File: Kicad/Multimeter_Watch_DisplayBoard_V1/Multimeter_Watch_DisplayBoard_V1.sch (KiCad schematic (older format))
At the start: 14 parts, among them J4 Conn_01x16_Female, J5 Conn_01x16_Female, Q1 A03400A N-MOS

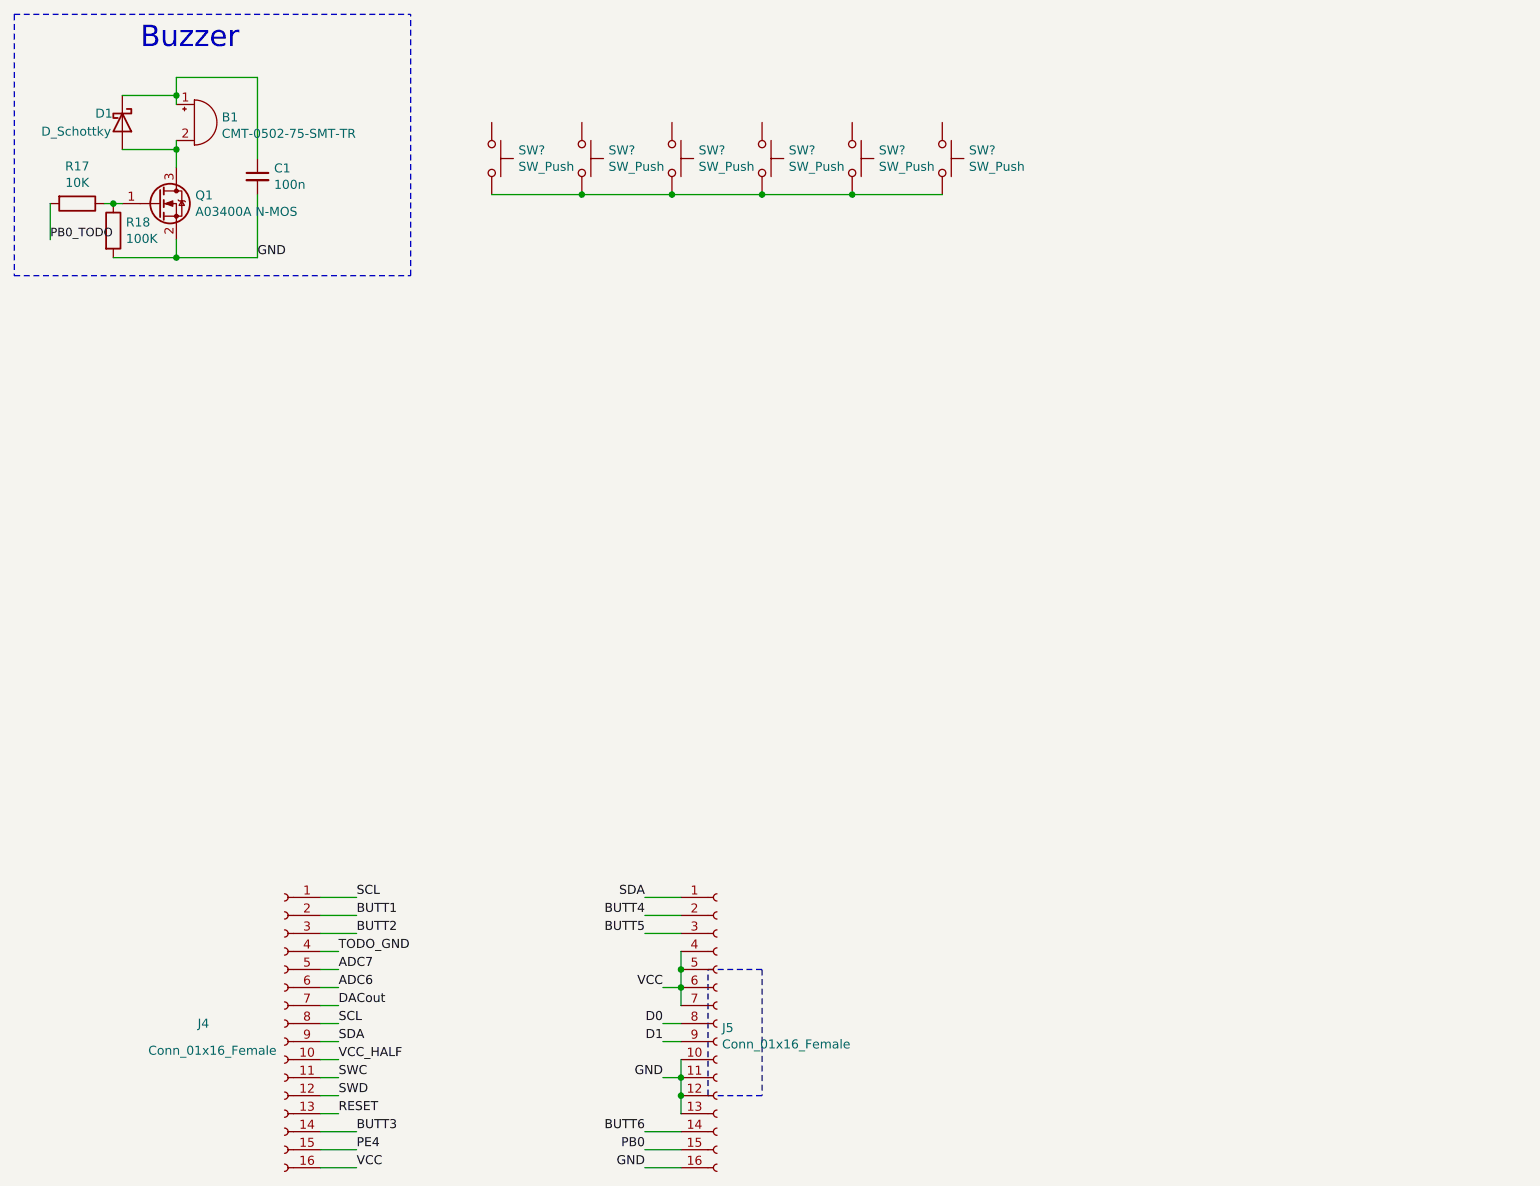
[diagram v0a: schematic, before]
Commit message: measure header distance by center of hole (courtyards are not symmetrical)
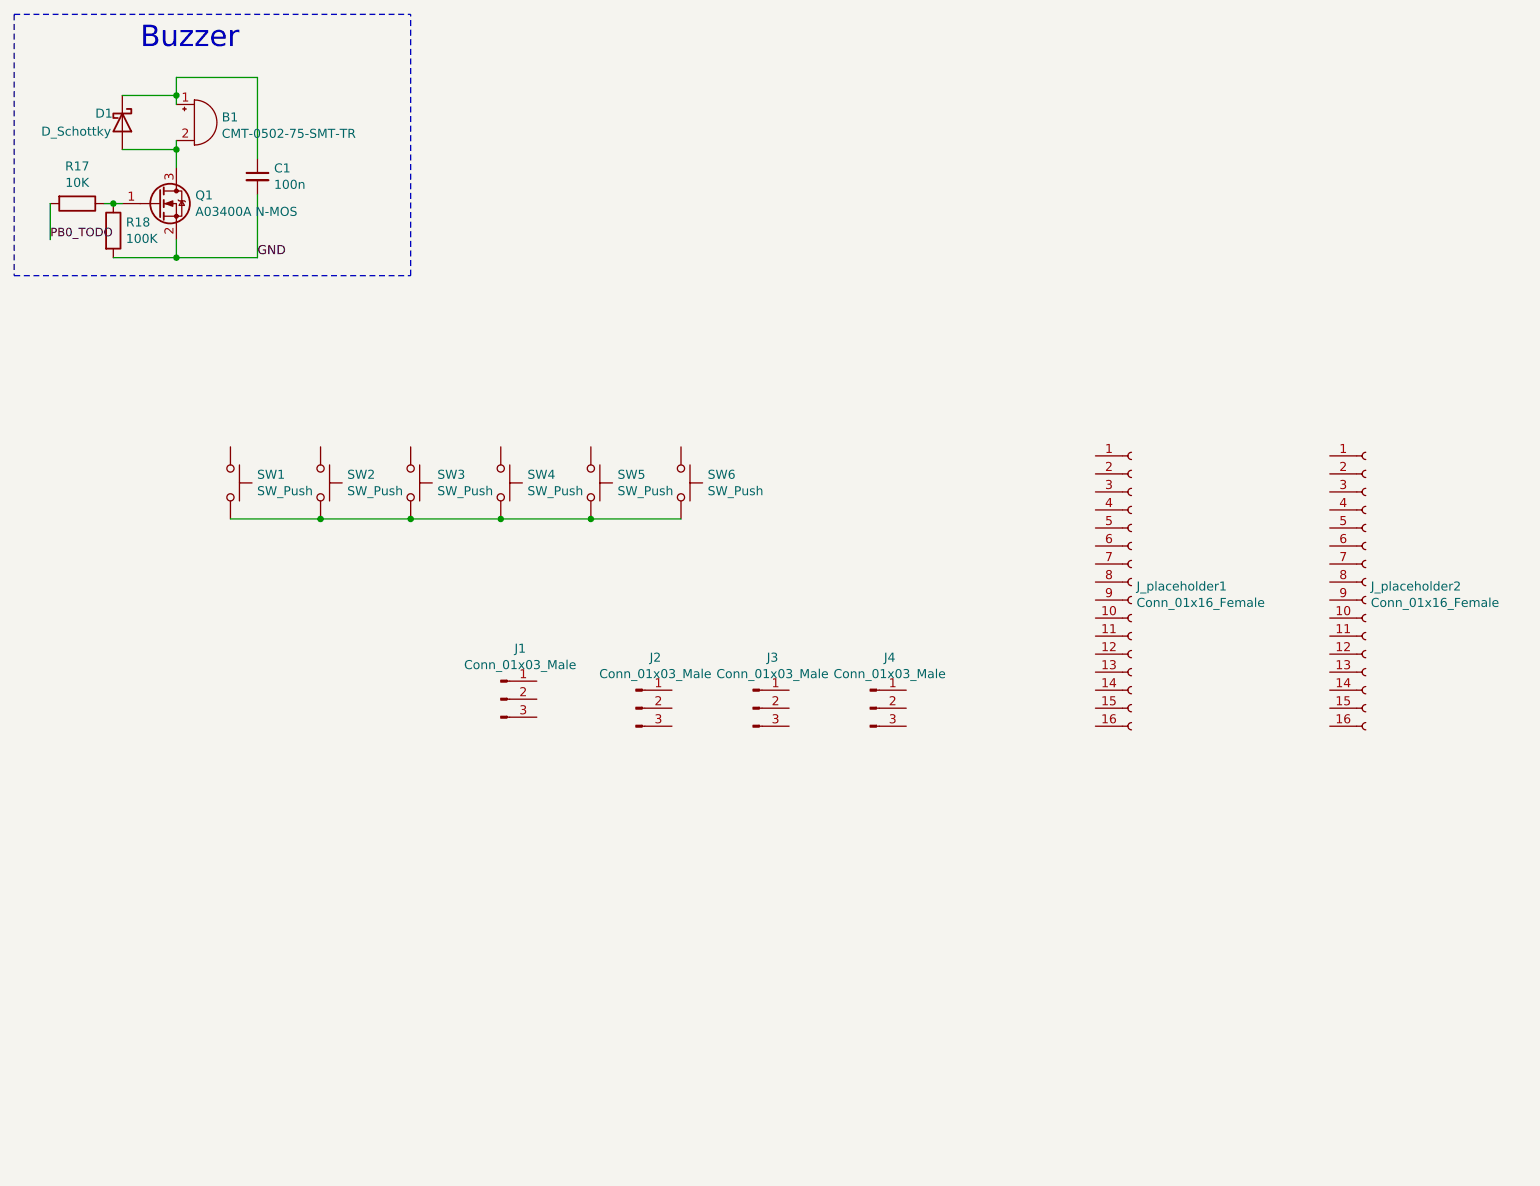
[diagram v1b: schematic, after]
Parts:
- removed J4, J5: Conn_01x16_Female, Connector_PinSocket_2.54mm:PinSocket_1x16_P2.54mm_Vertical, symbol Connector:Conn_01x16_Female
- added J1, J2, J3, J4: Conn_01x03_Male, Connector_PinSocket_2.54mm:PinSocket_1x03_P2.54mm_Vertical, symbol Connector:Conn_01x03_Male
- added J_placeholder1, J_placeholder2: Conn_01x16_Female, Connector_PinSocket_2.54mm:PinSocket_1x16_P2.54mm_Vertical, symbol Connector:Conn_01x16_Female
- gave numbers to parts that had none: 6
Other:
- moved on the sheet: SW1, SW2, SW3, SW4, SW5, SW6

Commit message: display board done, todo: move display down to allow for jack labels
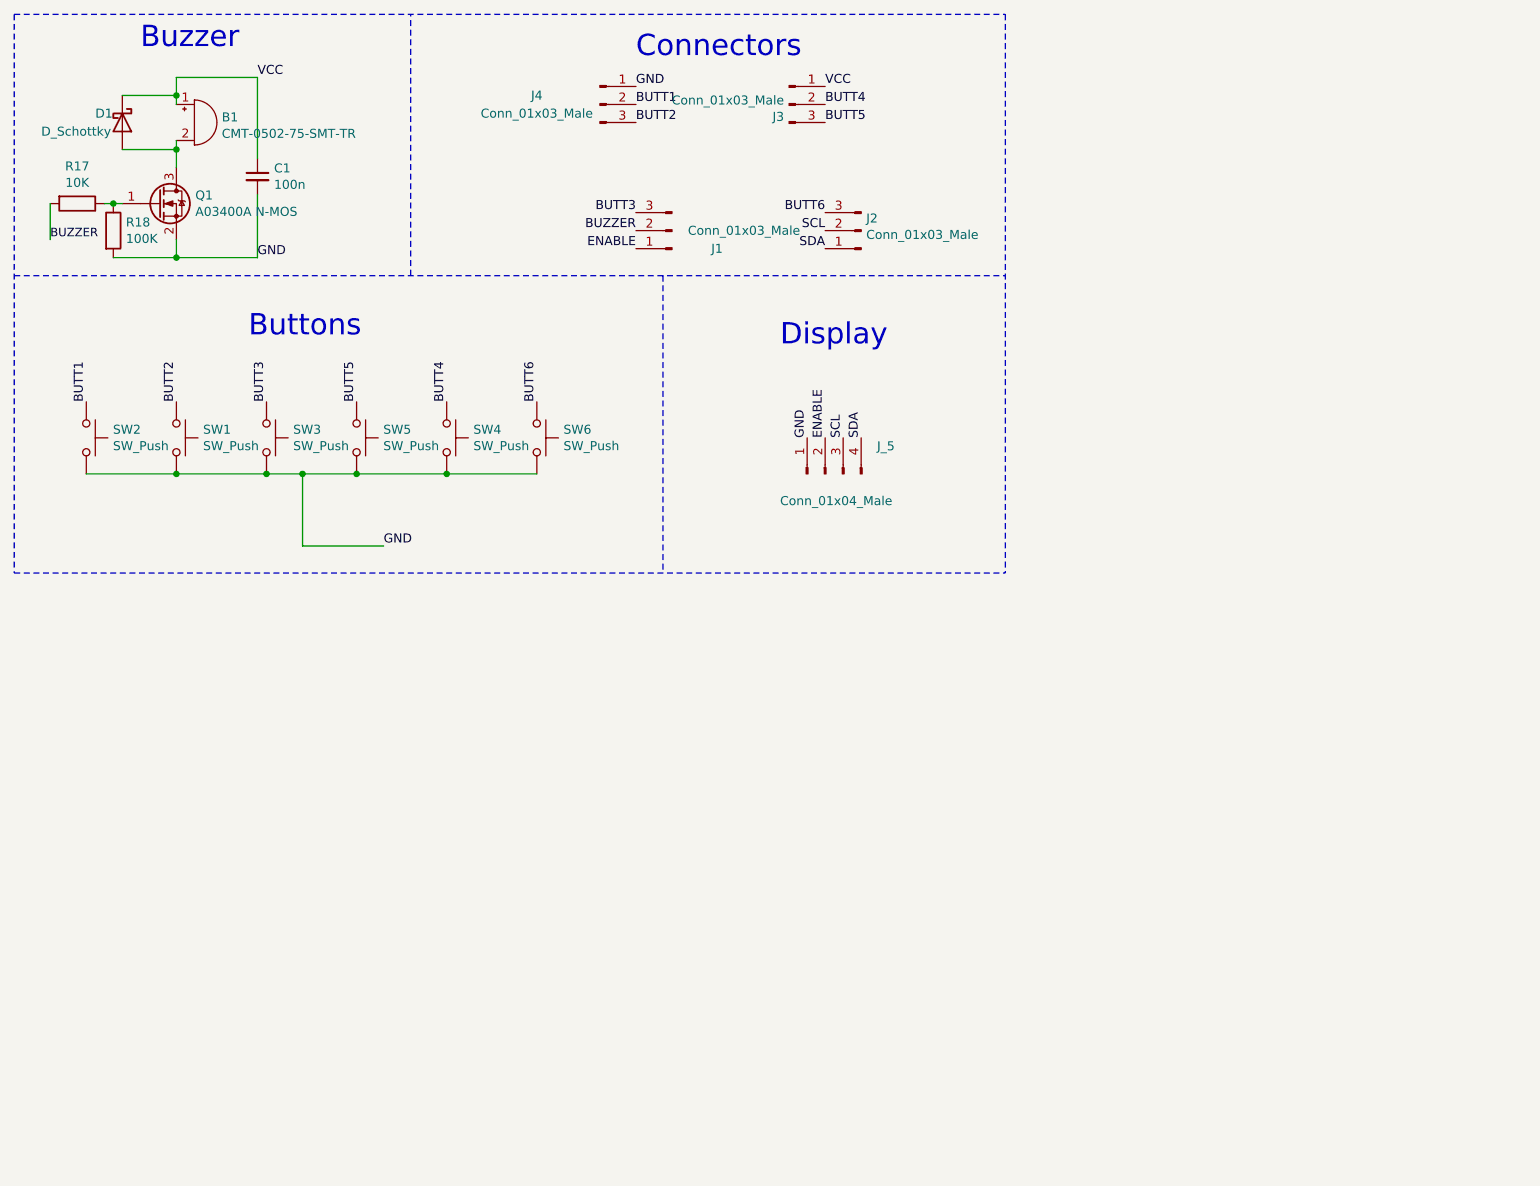
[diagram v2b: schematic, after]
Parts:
- removed J_placeholder1, J_placeholder2: Conn_01x16_Female, Connector_PinSocket_2.54mm:PinSocket_1x16_P2.54mm_Vertical, symbol Connector:Conn_01x16_Female
- added J_5: Conn_01x04_Male, Connector_PinSocket_2.54mm:PinSocket_1x04_P2.54mm_Vertical, symbol Connector:Conn_01x04_Male
- B1: footprint (none) -> Multimeter_Watch_custom_footprints:CMT-0502-75-SMT-TR
- C1: footprint (none) -> Capacitor_SMD:C_0603_1608Metric_Pad1.05x0.95mm_HandSolder
- D1: footprint (none) -> Diode_SMD:D_0805_2012Metric_Pad1.15x1.40mm_HandSolder
- R17, R18: footprint (none) -> Resistor_SMD:R_0805_2012Metric_Pad1.15x1.40mm_HandSolder
- SW1, SW2, SW3, SW4, SW5, SW6: footprint (none) -> Multimeter_Watch_custom_footprints:TVCM04N
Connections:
- net PB0_TODO is gone; now on net BUZZER: R17.2
- net GND: now also J4.1 (Pin_1), SW1.2, SW2.2, SW3.2, SW4.2, SW5.2, SW6.2, J_5.1 (Pin_1)
- net BUTT1: now reaches J4.2 (Pin_2)
- net BUTT1: now also SW2.1
- net BUTT2: now reaches J4.3 (Pin_3)
- net BUTT2: now also SW1.1
- net VCC: now reaches J3.1 (Pin_1)
- net VCC: now also B1.1 (-), C1.1, D1.1 (K)
- net BUTT4: now reaches J3.2 (Pin_2)
- net BUTT4: now also SW4.1
- net BUTT5: now reaches J3.3 (Pin_3)
- net BUTT5: now also SW5.1
- net SDA: now reaches J2.1 (Pin_1)
- net SDA: now also J_5.4 (Pin_4)
- net SCL: now reaches J2.2 (Pin_2)
- net SCL: now also J_5.3 (Pin_3)
- net BUTT6: now reaches J2.3 (Pin_3)
- net BUTT6: now also SW6.1
- net ENABLE: now reaches J1.1 (Pin_1)
- net ENABLE: now also J_5.2 (Pin_2)
- net BUZZER: now reaches J1.2 (Pin_2)
- net BUTT3: now reaches J1.3 (Pin_3)
- net BUTT3: now also SW3.1
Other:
- note added: "Buttons"
- note added: "Connectors"
- note added: "Display"
- moved on the sheet: J1, J2, J3, J4, SW1, SW2, SW3, SW4, SW5, SW6
